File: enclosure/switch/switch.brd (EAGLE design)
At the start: 37 x 21 mm, 10 parts, among them SW1 TVGP01-G73BB

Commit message: [update] brdを作製
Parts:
- moved U$3 74.8 mm to (34.0, 17.0), turned to 270 degrees
- moved R4 73.3 mm to (30.0, 22.5), turned to 90 degrees
- moved LED2 68.7 mm to (24.5, 9.00), turned to 90 degrees
- moved R2 61.1 mm to (30.0, 11.5), turned to 90 degrees
- moved R1 58.7 mm to (7.00, 11.5), turned to 90 degrees
- moved U$2 55.5 mm to (18.5, 33.0)
- moved U$1 49.5 mm to (18.5, 29.0)
- moved LED1 49.2 mm to (12.5, 9.00), turned to 90 degrees
- moved SW1 44.3 mm to (18.5, 21.0)
- moved R3 44.2 mm to (7.00, 22.5), turned to 270 degrees
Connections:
- net +3V3: now also U$1.P$1; no longer U$1.P$2
- net +5V: now also U$1.P$2; no longer U$1.P$1
- net GND: now also U$1.P$3; no longer U$1.P$8
- net N$3: now also U$1.P$6; no longer U$1.P$7
- net N$4: now also U$1.P$5; no longer U$1.P$6
- net N$5: now also U$1.P$7; no longer U$1.P$5
- net N$6: now also U$1.P$8; no longer U$1.P$3
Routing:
- net GND: track 0.00 -> 59.1 mm
- net N$4: track 0.00 -> 33.9 mm
- net N$3: track 0.00 -> 31.8 mm
- net N$5: track 0.00 -> 25.3 mm
- net +3V3: track 0.00 -> 25.3 mm
- net N$6: track 0.00 -> 15.6 mm
- net +5V: track 0.00 -> 11.5 mm
- net N$2: track 0.00 -> 9.86 mm
- net N$1: track 0.00 -> 9.86 mm
- net N$8: track 0.00 -> 4.53 mm
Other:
- board size 37 x 21 mm -> 37 x 37 mm

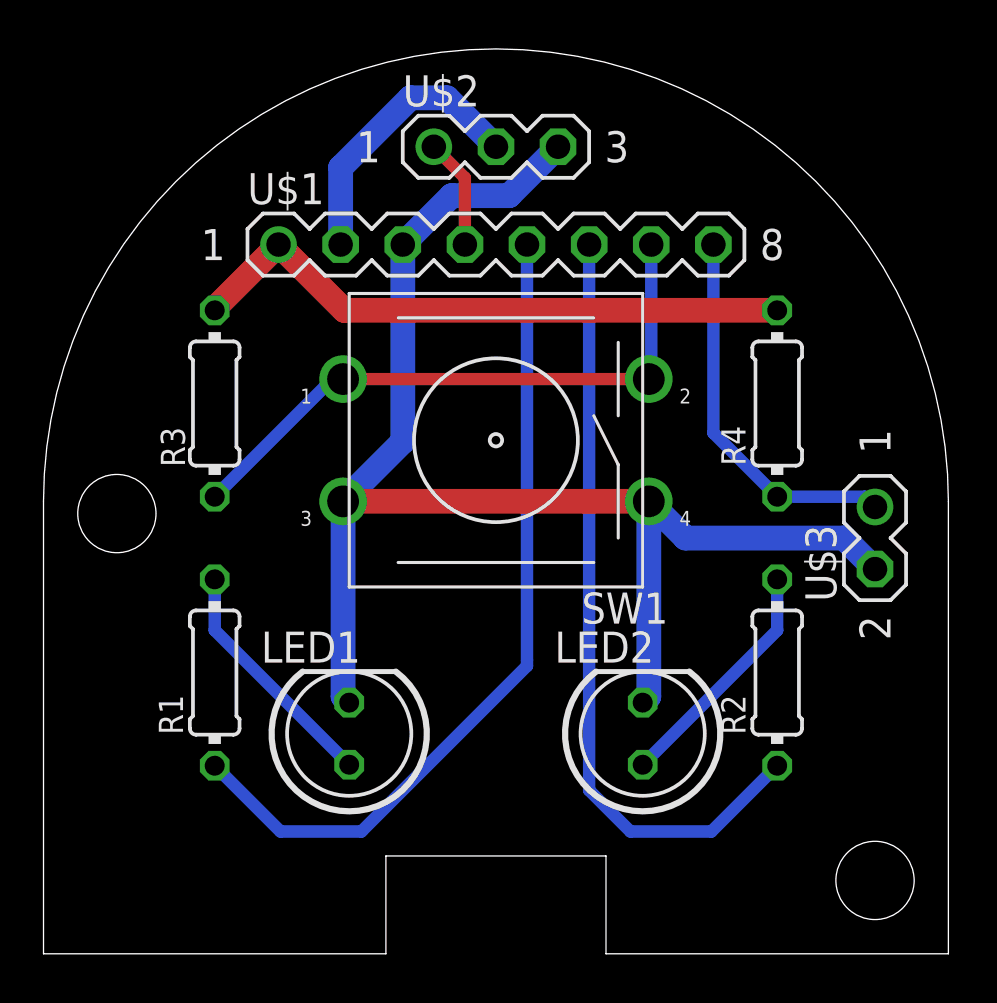
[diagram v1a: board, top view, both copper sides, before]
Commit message: [update] コネクタをPHにして裏に部品を実装するようにした
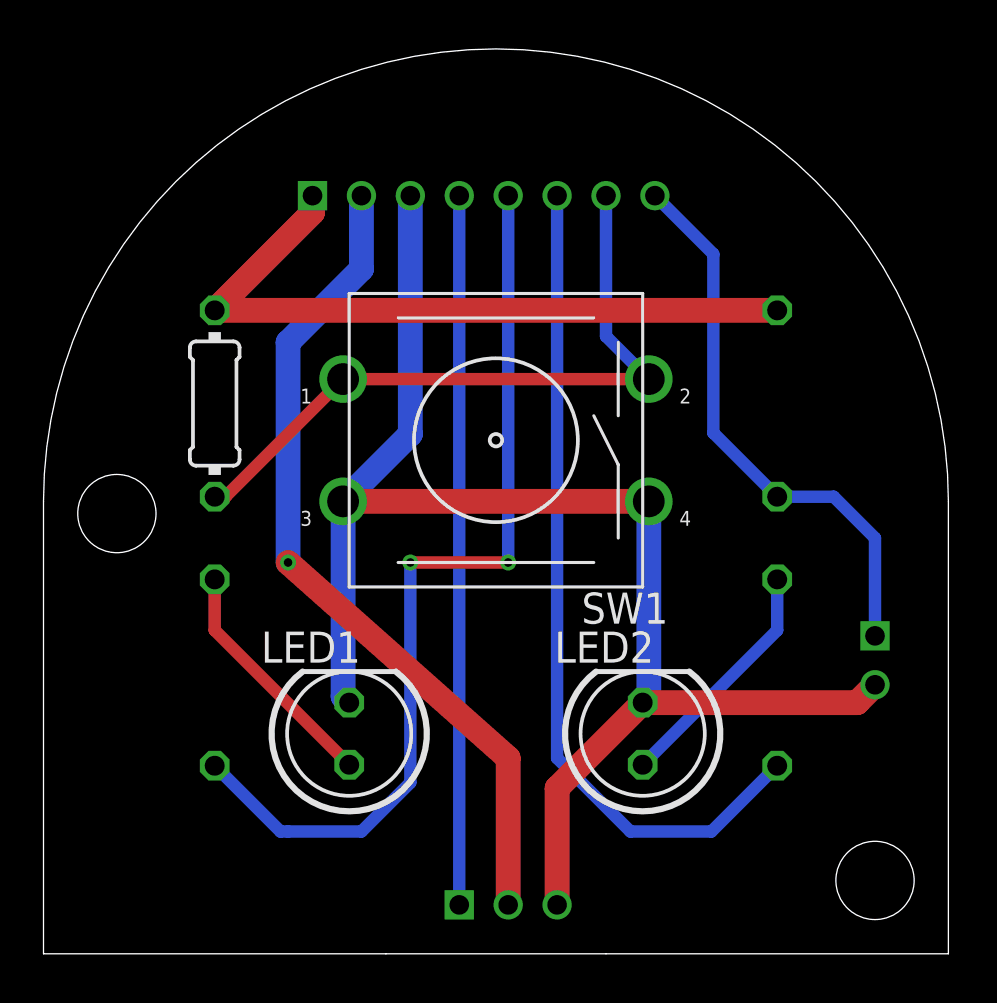
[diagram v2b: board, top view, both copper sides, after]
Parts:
- removed U$1: PIN_HEADER_MALE_1X08_08P, 180118 Library by matsu:PIN_HEADER_MALE_1X08_08P
- removed U$2: PIN_HEADER_MALE_1X03_03P, 180118 Library by matsu:PIN_HEADER_MALE_1X03_03P
- removed U$3: PIN_HEADER_MALE_1X02_02P, 180118 Library by matsu:PIN_HEADER_MALE_1X02_02P
- added CN1: (no value), jst-ph:B8B-PH-K-S
- added CN2: (no value), jst-ph:B2B-PH-K-S
- added CN3: (no value), jst-ph:B3B-PH-K-S
- flipped R1 to the bottom
- flipped R2 to the bottom
- flipped R4 to the bottom
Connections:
- net +3V3: now also CN1.1; no longer U$1.P$1
- net +5V: now also CN1.2, CN3.2; no longer U$1.P$2, U$2.P$2
- net GND: now also CN1.3, CN2.2, CN3.3; no longer U$1.P$3, U$2.P$3, U$3.P$2
- net N$3: now also CN1.6; no longer U$1.P$6
- net N$4: now also CN1.5; no longer U$1.P$5
- net N$5: now also CN1.7; no longer U$1.P$7
- net N$6: now also CN1.8, CN2.1; no longer U$1.P$8, U$3.P$1
- net N$8: now also CN1.4, CN3.1; no longer U$1.P$4, U$2.P$1
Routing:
- net N$8: track 4.53 -> 29.0 mm
- net +5V: track 11.5 -> 34.3 mm, vias 0 -> 1
- net N$6: track 15.6 -> 23.1 mm
- net +3V3: track 25.3 -> 29.3 mm
- net N$4: track 33.9 -> 37.9 mm, vias 0 -> 2
- net GND: track 59.1 -> 62.3 mm
- net N$5: track 25.3 -> 28.0 mm
- net N$3: track 31.8 -> 34.4 mm
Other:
- outline, holes or cut-outs redrawn
- board text added: "Kagisys rev.2.0 Procon Seminar Designed by @sumizome0213"

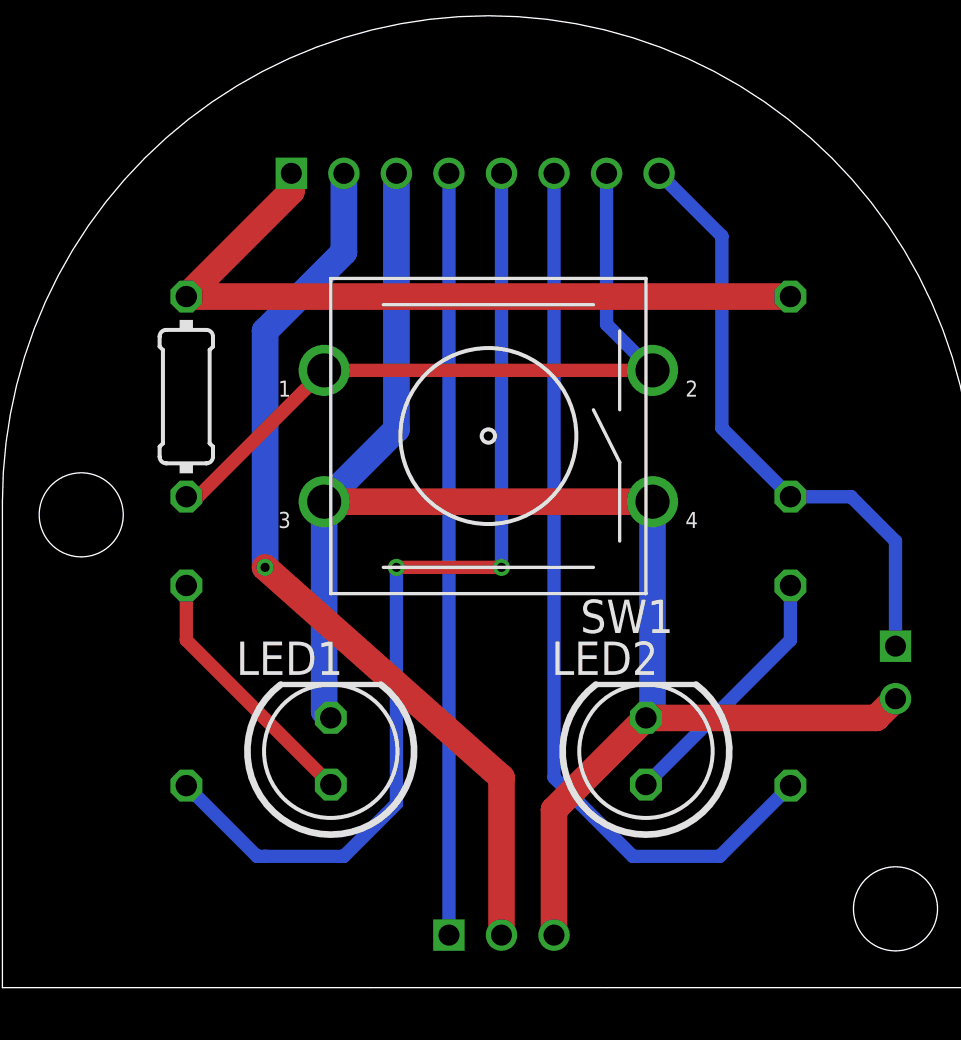
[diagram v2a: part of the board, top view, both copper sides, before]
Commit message: [fix] シルク・位置ずれを解消
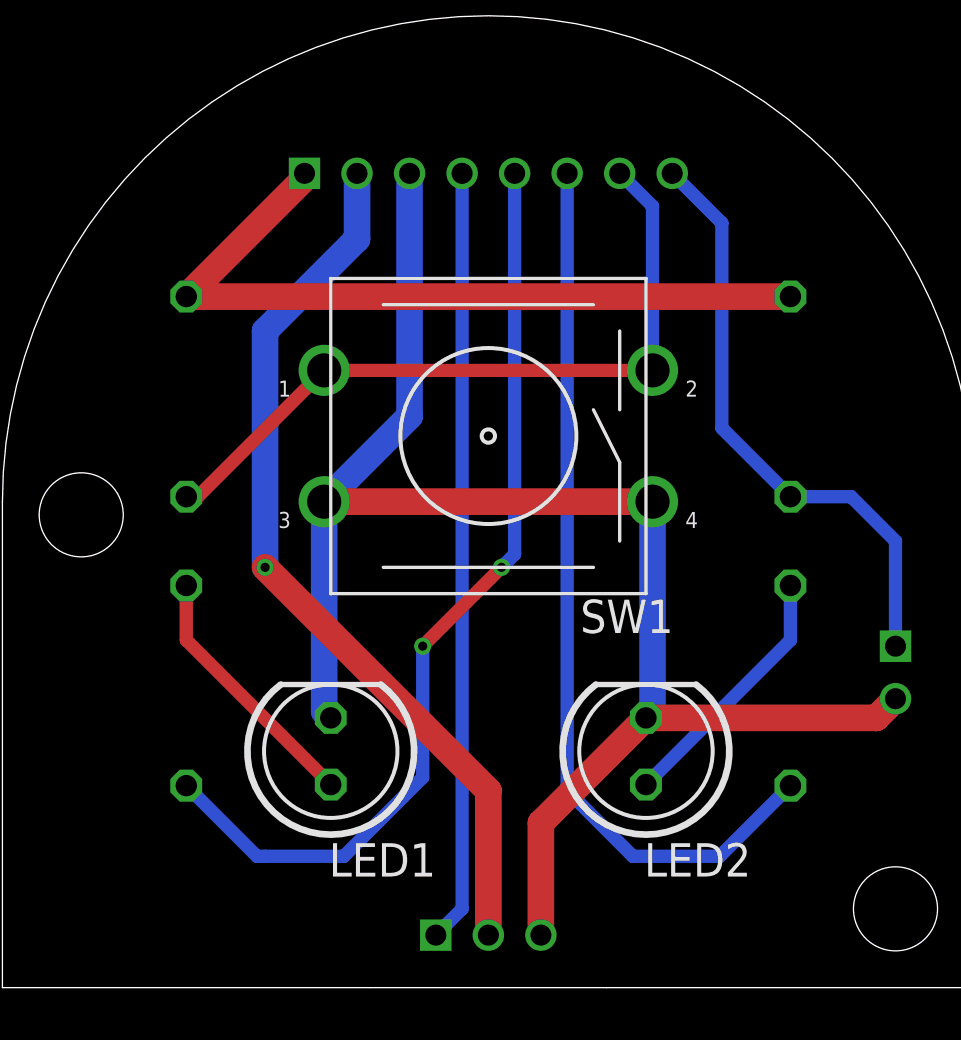
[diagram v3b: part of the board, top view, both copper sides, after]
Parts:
- moved CN1 0.50 mm to (18.5, 31.0)
- moved CN3 0.50 mm to (18.5, 2.00)
- flipped R3 to the bottom
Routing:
- net N$4: track 37.9 -> 35.8 mm
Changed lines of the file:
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@@
 <setting verticaltext="up"/>
 </settings>
-<grid distance="39.3700787" unitdist="mil" unit="mil" style="lines" multiple="1" display="yes" altdistance="0.5" altunitdist="mm" altunit="mm"/>
+<grid distance="1" unitdist="mm" unit="mm" style="lines" multiple="1" display="yes" altdistance="0.5" altunitdist="mm" altunit="mm"/>
 <layers>
 <layer number="1" name="Top" color="4" fill="1" visible="yes" active="yes"/>
@@
 <wire x1="0" y1="18.5" x2="37" y2="18.5" width="0" layer="20" curve="-180"/>
 <wire x1="14" y1="0" x2="23" y2="0" width="0" layer="20"/>
-<text x="12" y="0.5" size="0.889" layer="22" rot="MR0">        Kagisys rev.2.0
+<text x="13" y="0.5" size="0.889" layer="22" rot="MR0">        Kagisys rev.2.0
        Procon Seminar
 Designed by
@@
 <elements>
 <element name="LED1" library="180118 Library by matsu" package="LED5MM" value="" x="12.5" y="9" smashed="yes" rot="R90">
-<attribute name="NAME" x="12.9666" y="13.175" size="1.27" layer="25" ratio="10" rot="R180"/>
+<attribute name="NAME" x="16.5" y="5.5" size="1.27" layer="25" ratio="10" rot="R180"/>
 <attribute name="VALUE" x="14.3034" y="12.2004" size="1.27" layer="27" ratio="10" rot="R90"/>
 </element>
 <element name="LED2" library="180118 Library by matsu" package="LED5MM" value="" x="24.5" y="9" smashed="yes" rot="R90">
-<attribute name="NAME" x="24.9666" y="13.175" size="1.27" layer="25" ratio="10" rot="R180"/>
+<attribute name="NAME" x="28.5" y="5.5" size="1.27" layer="25" ratio="10" rot="R180"/>
 <attribute name="VALUE" x="26.3034" y="12.2004" size="1.27" layer="27" ratio="10" rot="R90"/>
 </element>
 <element name="R1" library="180118 Library by matsu" package="0204/7" value="" x="7" y="11.5" rot="SMR90"/>
 <element name="R2" library="180118 Library by matsu" package="0204/7" value="" x="30" y="11.5" rot="MR90"/>
-<element name="R3" library="180118 Library by matsu" package="0204/7" value="" x="7" y="22.5" smashed="yes" rot="R270">
-<attribute name="NAME" x="9.5" y="21.5" size="0.9906" layer="26" ratio="10" rot="MR270"/>
-<attribute name="VALUE" x="6.5174" y="24.1256" size="0.9906" layer="27" ratio="10" rot="R270"/>
+<element name="R3" library="180118 Library by matsu" package="0204/7" value="" x="7" y="22.5" smashed="yes" rot="MR270">
+<attribute name="NAME" x="9.3" y="21.7" size="0.9906" layer="26" ratio="10" rot="MR270"/>
+<attribute name="VALUE" x="7.4826" y="24.1256" size="0.9906" layer="28" ratio="10" rot="MR270"/>
 </element>
 <element name="R4" library="180118 Library by matsu" package="0204/7" value="" x="30" y="22.5" rot="MR90"/>
@@
 <attribute name="NAME" x="22" y="13.5" size="1.27" layer="25" ratio="10"/>
 </element>
-<element name="CN1" library="jst-ph" package="B8B-PH-K-S" value="" x="18" y="31" smashed="yes" rot="MR180">
-<attribute name="NAME" x="9" y="28.5" size="1.27" layer="26" ratio="10" rot="MR180"/>
-<attribute name="VALUE" x="9" y="35.5" size="1.27" layer="28" rot="MR180"/>
+<element name="CN1" library="jst-ph" package="B8B-PH-K-S" value="" x="18.5" y="31" smashed="yes" rot="MR180">
+<attribute name="NAME" x="9.5" y="28.5" size="1.27" layer="26" ratio="10" rot="MR180"/>
+<attribute name="VALUE" x="9.5" y="35.5" size="1.27" layer="28" rot="MR180"/>
 </element>
 <element name="CN2" library="jst-ph" package="B2B-PH-K-S" value="" x="34" y="12" smashed="yes" rot="SMR270">
-<attribute name="NAME" x="33.5" y="9" size="1.27" layer="26" ratio="10" rot="MR270"/>
+<attribute name="NAME" x="33.5" y="8.8" size="1.27" layer="26" ratio="10" rot="MR270"/>
 <attribute name="VALUE" x="38.5" y="15" size="1.27" layer="28" rot="SMR270"/>
 </element>
-<element name="CN3" library="jst-ph" package="B3B-PH-K-S" value="" x="19" y="2" smashed="yes" rot="SMR180">
-<attribute name="NAME" x="23" y="1.5" size="1.27" layer="26" ratio="10" rot="MR180"/>
-<attribute name="VALUE" x="15" y="6.5" size="1.27" layer="28" rot="SMR180"/>
+<element name="CN3" library="jst-ph" package="B3B-PH-K-S" value="" x="18.5" y="2" smashed="yes" rot="SMR180">
+<attribute name="NAME" x="22.7" y="1.5" size="1.27" layer="26" ratio="10" rot="MR180"/>
+<attribute name="VALUE" x="14.5" y="6.5" size="1.27" layer="28" rot="SMR180"/>
 </element>
 </elements>
@@
 <contactref element="R4" pad="2"/>
 <contactref element="CN1" pad="1"/>
-<wire x1="7" y1="26.31" x2="30" y2="26.31" width="1.016" layer="1"/>
-<wire x1="7" y1="26.31" x2="11" y2="30.31" width="1.016" layer="1"/>
-<wire x1="11" y1="30.31" x2="11" y2="31" width="1.016" layer="1"/>
+<wire x1="30" y1="26.31" x2="7" y2="26.31" width="1.016" layer="1"/>
+<wire x1="7" y1="26.31" x2="11.5" y2="30.81" width="1.016" layer="1"/>
+<wire x1="11.5" y1="30.81" x2="11.5" y2="31" width="1.016" layer="1"/>
 </signal>
 <signal name="GND" class="1">
@@
 <contactref element="CN3" pad="3"/>
 <contactref element="CN1" pad="3"/>
-<wire x1="24.5" y1="10.27" x2="21" y2="6.77" width="1.016" layer="1"/>
-<wire x1="15" y1="21.25" x2="12.25" y2="18.5" width="1.016" layer="16"/>
-<wire x1="21" y1="6.77" x2="21" y2="2" width="1.016" layer="1"/>
 <wire x1="24.5" y1="10.27" x2="33.27" y2="10.27" width="1.016" layer="1"/>
 <wire x1="33.27" y1="10.27" x2="34" y2="11" width="1.016" layer="1"/>
-<wire x1="15" y1="31" x2="15" y2="21.25" width="1.016" layer="16"/>
+<wire x1="15.5" y1="31" x2="15.5" y2="21.75" width="1.016" layer="16"/>
+<wire x1="15.5" y1="21.75" x2="12.25" y2="18.5" width="1.016" layer="16"/>
+<wire x1="20.5" y1="2" x2="20.5" y2="6.27" width="1.016" layer="1"/>
+<wire x1="20.5" y1="6.27" x2="24.5" y2="10.27" width="1.016" layer="1"/>
 </signal>
 <signal name="N$4">
 <contactref element="R1" pad="1"/>
 <contactref element="CN1" pad="5"/>
-<via x="19" y="16" extent="1-16" drill="0.35"/>
-<wire x1="19" y1="16" x2="15" y2="16" width="0.508" layer="1"/>
-<via x="15" y="16" extent="1-16" drill="0.35"/>
-<wire x1="15" y1="16" x2="15" y2="7" width="0.508" layer="16"/>
-<wire x1="15" y1="7" x2="13" y2="5" width="0.508" layer="16"/>
 <wire x1="13" y1="5" x2="10" y2="5" width="0.508" layer="16"/>
 <wire x1="9.69" y1="5" x2="10" y2="5" width="0.508" layer="16"/>
 <wire x1="7" y1="7.69" x2="9.69" y2="5" width="0.508" layer="16"/>
-<wire x1="19" y1="31" x2="19" y2="16" width="0.508" layer="16"/>
+<wire x1="19.5" y1="31" x2="19.5" y2="16.5" width="0.508" layer="16"/>
+<wire x1="19.5" y1="16.5" x2="19" y2="16" width="0.508" layer="16"/>
+<via x="19" y="16" extent="1-16" drill="0.35"/>
+<wire x1="19" y1="16" x2="16" y2="13" width="0.508" layer="1"/>
+<via x="16" y="13" extent="1-16" drill="0.35"/>
+<wire x1="16" y1="13" x2="16" y2="8" width="0.508" layer="16"/>
+<wire x1="16" y1="8" x2="13" y2="5" width="0.508" layer="16"/>
 </signal>
 <signal name="N$1">
@@
 <wire x1="12.25" y1="23.5" x2="24.75" y2="23.5" width="0.508" layer="1"/>
 <contactref element="CN1" pad="7"/>
-<wire x1="23" y1="25.25" x2="24.75" y2="23.5" width="0.508" layer="16"/>
 <wire x1="12.25" y1="23.5" x2="7.44" y2="18.69" width="0.508" layer="1"/>
 <wire x1="7.44" y1="18.69" x2="7" y2="18.69" width="0.508" layer="1"/>
-<wire x1="23" y1="31" x2="23" y2="25.25" width="0.508" layer="16"/>
+<wire x1="23.5" y1="31" x2="24.75" y2="29.75" width="0.508" layer="16"/>
+<wire x1="24.75" y1="29.75" x2="24.75" y2="23.5" width="0.508" layer="16"/>
 </signal>
 <signal name="N$6">
@@
 <contactref element="CN2" pad="1"/>
 <contactref element="CN1" pad="8"/>
-<wire x1="27.39" y1="21.3" x2="27.39" y2="28.61" width="0.508" layer="16"/>
 <wire x1="34" y1="13" x2="34" y2="17" width="0.508" layer="16"/>
 <wire x1="32.31" y1="18.69" x2="30" y2="18.69" width="0.508" layer="16"/>
 <wire x1="34" y1="17" x2="32.31" y2="18.69" width="0.508" layer="16"/>
-<wire x1="30" y1="18.69" x2="27.39" y2="21.3" width="0.508" layer="16"/>
-<wire x1="27.39" y1="28.61" x2="25" y2="31" width="0.508" layer="16"/>
+<wire x1="27.39" y1="21.3" x2="30" y2="18.69" width="0.508" layer="16"/>
+<wire x1="25.5" y1="31" x2="27.39" y2="29.11" width="0.508" layer="16"/>
+<wire x1="27.39" y1="29.11" x2="27.39" y2="21.3" width="0.508" layer="16"/>
 </signal>
 <signal name="N$3">
 <contactref element="R2" pad="1"/>
-<wire x1="27.31" y1="5" x2="24" y2="5" width="0.508" layer="16"/>
+<wire x1="24" y1="5" x2="27.31" y2="5" width="0.508" layer="16"/>
 <contactref element="CN1" pad="6"/>
-<wire x1="24" y1="5" x2="21" y2="8" width="0.508" layer="16"/>
 <wire x1="30" y1="7.69" x2="27.31" y2="5" width="0.508" layer="16"/>
-<wire x1="21" y1="8" x2="21" y2="31" width="0.508" layer="16"/>
+<wire x1="21.5" y1="31" x2="21.5" y2="7.5" width="0.508" layer="16"/>
+<wire x1="21.5" y1="7.5" x2="24" y2="5" width="0.508" layer="16"/>
 </signal>
 <signal name="+5V" class="1">
 <contactref element="CN3" pad="2"/>
 <contactref element="CN1" pad="2"/>
-<wire x1="13" y1="28" x2="10" y2="25" width="1.016" layer="16"/>
-<wire x1="10" y1="16" x2="19" y2="8" width="1.016" layer="1"/>
 <via x="10" y="16" extent="1-16" drill="0.35"/>
 <wire x1="10" y1="25" x2="10" y2="16" width="1.016" layer="16"/>
-<wire x1="19" y1="8" x2="19" y2="2" width="1.016" layer="1"/>
-<wire x1="13" y1="31" x2="13" y2="28" width="1.016" layer="16"/>
+<wire x1="13.5" y1="31" x2="13.5" y2="28.5" width="1.016" layer="16"/>
+<wire x1="13.5" y1="28.5" x2="10" y2="25" width="1.016" layer="16"/>
+<wire x1="10" y1="16" x2="18.5" y2="7.5" width="1.016" layer="1"/>
+<wire x1="18.5" y1="7.5" x2="18.5" y2="2" width="1.016" layer="1"/>
 </signal>
 <signal name="N$8">
 <contactref element="CN3" pad="1"/>
 <contactref element="CN1" pad="4"/>
-<wire x1="17" y1="2" x2="17" y2="31" width="0.508" layer="16"/>
+<wire x1="17.5" y1="31" x2="17.5" y2="3" width="0.508" layer="16"/>
+<wire x1="17.5" y1="3" x2="16.5" y2="2" width="0.508" layer="16"/>
 </signal>
 </signals>
